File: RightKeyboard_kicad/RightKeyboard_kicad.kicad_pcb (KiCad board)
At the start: 2 copper layers, 139.8 x 88.1 mm, 37 parts, among them U1 Arduino_Pro_Micro

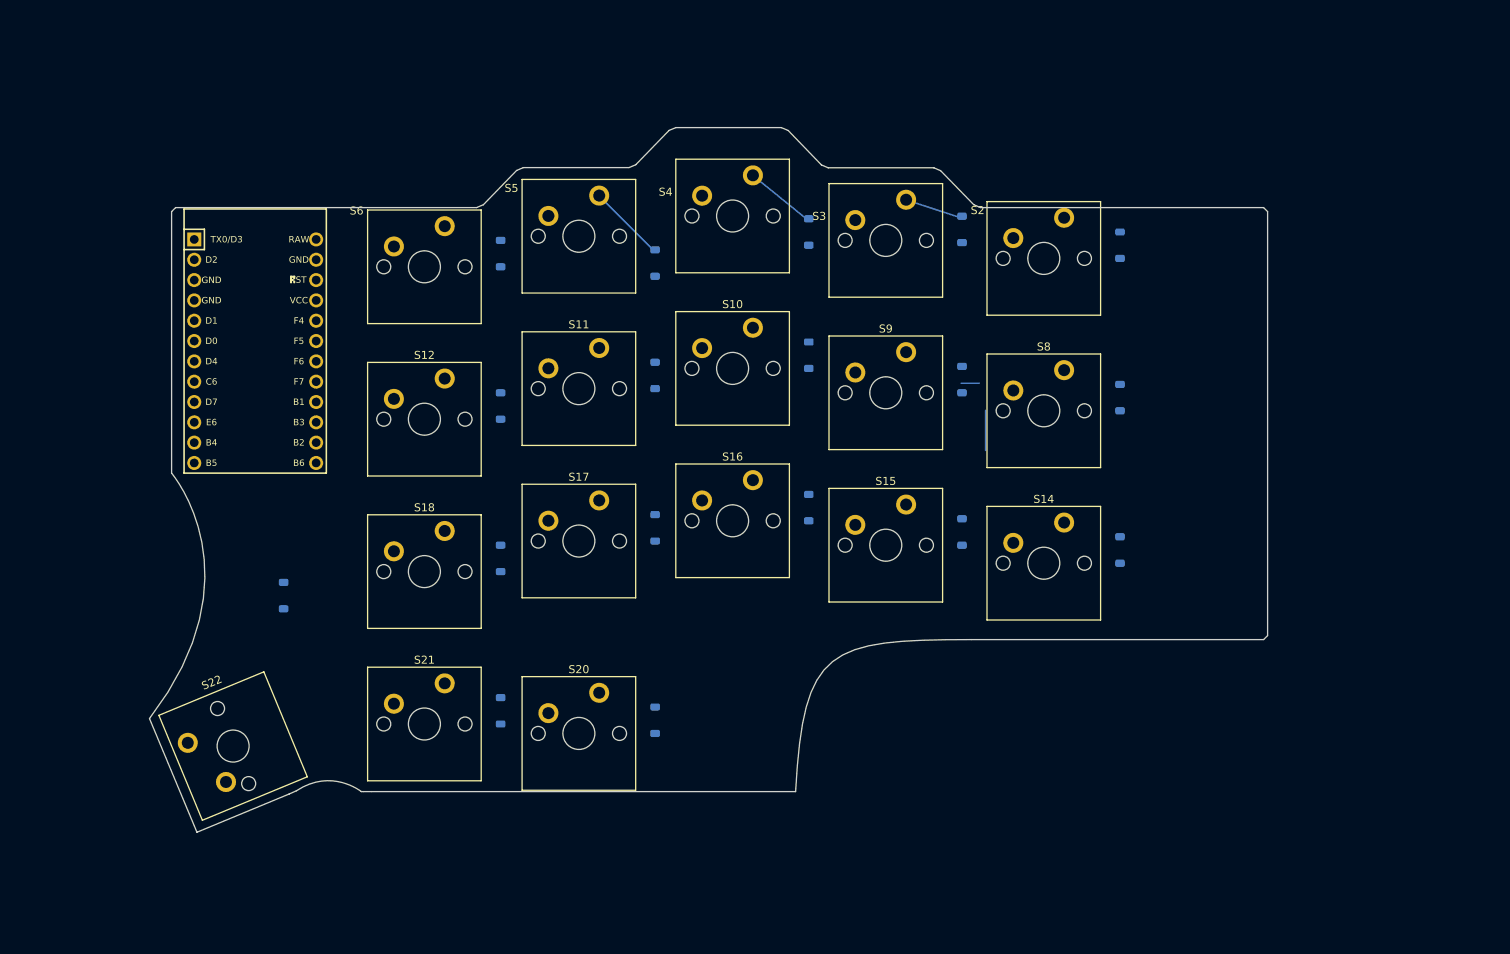
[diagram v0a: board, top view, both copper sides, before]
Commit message: Finished Right Keyboard PCB
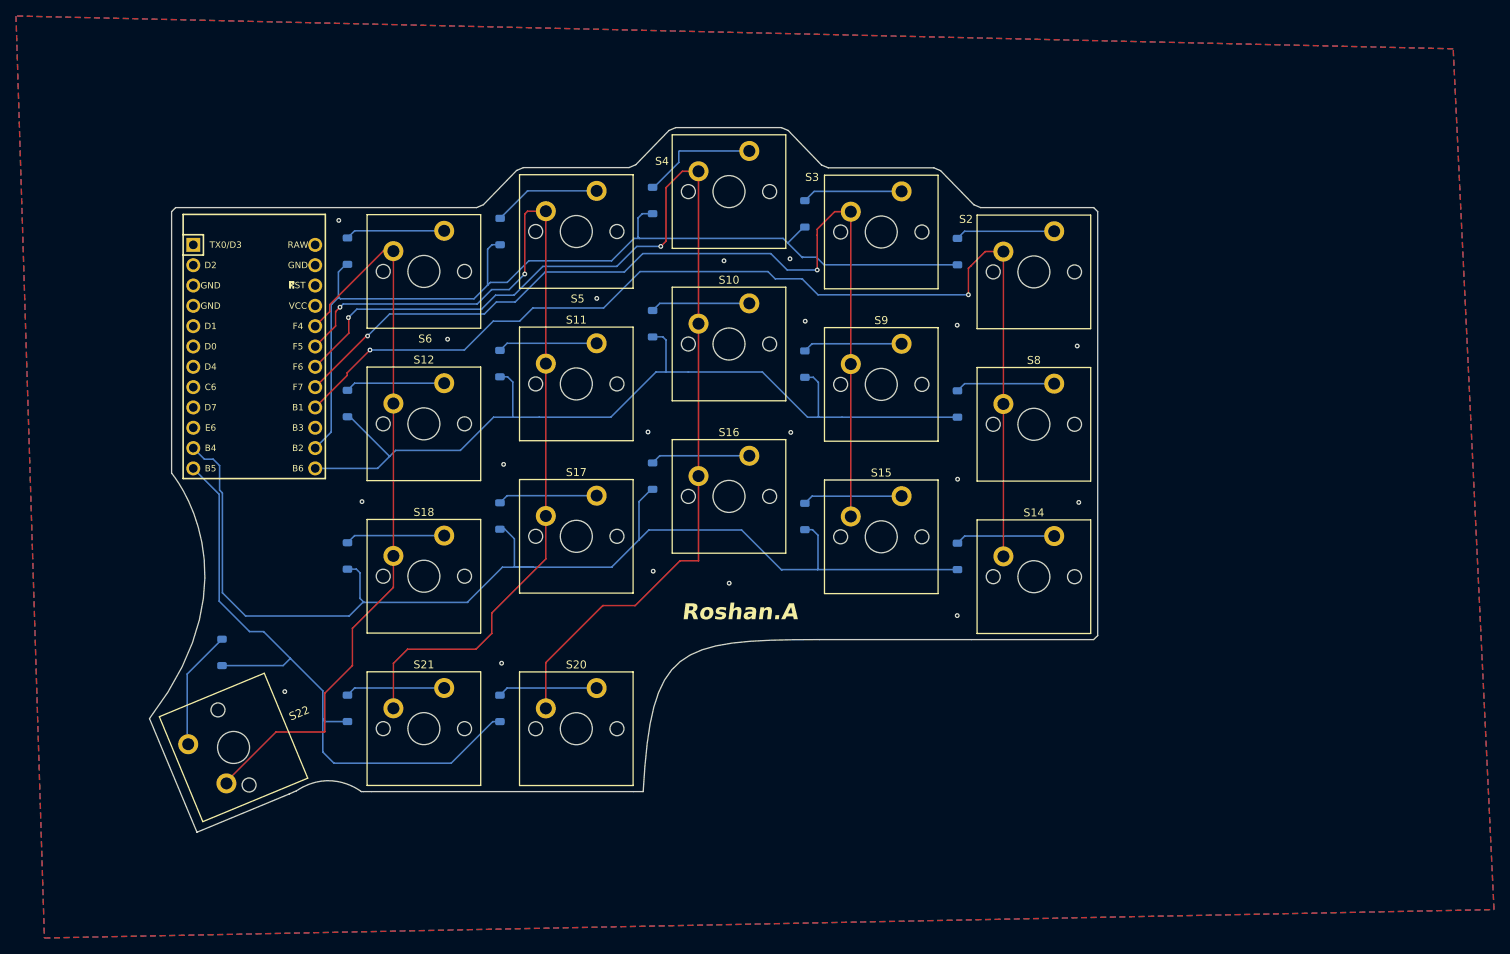
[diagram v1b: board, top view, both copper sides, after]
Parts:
- moved D14 20.3 mm to (165.4, 100.8)
- moved D2 20.3 mm to (165.4, 62.8)
- moved D8 20.3 mm to (165.4, 81.8)
- moved D10 19.9 mm to (127.3, 71.8)
- moved D16 19.9 mm to (127.3, 90.8)
- moved D4 19.9 mm to (127.3, 56.4)
- moved D5 19.8 mm to (108.3, 60.2)
- moved D15 19.7 mm to (146.4, 95.9)
- moved D3 19.7 mm to (146.4, 58.0)
- moved D9 19.7 mm to (146.4, 76.8)
- moved D11 19.5 mm to (108.2, 76.8)
- moved D17 19.5 mm to (108.2, 95.8)
- moved D20 19.5 mm to (108.2, 119.9)
- moved D12 19.1 mm to (89.2, 81.7)
- moved D18 19.1 mm to (89.2, 100.8)
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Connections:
- S10 pad 1: /Col4 -> /Col3
- S11 pad 1: /Col5 -> /Col2
- S12 pad 1: /Col6 -> /Col1
- S14 pad 1: /Col2 -> /Col5
- S15 pad 1: /Col3 -> /Col4
- S16 pad 1: /Col4 -> /Col3
- S17 pad 1: /Col5 -> /Col2
- S18 pad 1: /Col6 -> /Col1
- S2 pad 1: /Col2 -> /Col5
- S20 pad 1: /Col4 -> /Col3
- S21 pad 1: /Col5 -> /Col2
- S22 pad 1: /Col6 -> /Col1
- S3 pad 1: /Col3 -> /Col4
- S4 pad 1: /Col4 -> /Col3
- S5 pad 1: /Col5 -> /Col2
- S6 pad 1: /Col6 -> /Col1
- S8 pad 1: /Col2 -> /Col5
- S9 pad 1: /Col3 -> /Col4
- U1 pad 10: /Col6 -> unconnected-(U1-7/PE6-Pad10)
- U1 pad 11: /Row1 -> /Row3
- U1 pad 12: /Row2 -> /Row4
- U1 pad 13: unconnected-(U1-10/PB6-Pad13) -> /Row2
- U1 pad 14: unconnected-(U1-16/PB2-Pad14) -> /Row1
- U1 pad 15: /Row3 -> /Col6
- U1 pad 16: /Row4 -> /Col5
- U1 pad 17: unconnected-(U1-A0/PF7-Pad17) -> /Col4
- U1 pad 18: unconnected-(U1-A1/PF6-Pad18) -> /Col3
- U1 pad 19: unconnected-(U1-A2/PF5-Pad19) -> /Col2
- U1 pad 20: unconnected-(U1-A3/PF4-Pad20) -> /Col1
- U1 pad 23: unconnected-(U1-GND-Pad23) -> /GND
- U1 pad 3: /GND -> unconnected-(U1-GND-Pad3)
- U1 pad 5: /Col1 -> unconnected-(U1-2/PD1-Pad5)
- U1 pad 6: /Col2 -> unconnected-(U1-3/PD0-Pad6)
- U1 pad 7: /Col3 -> unconnected-(U1-4/PD4-Pad7)
- U1 pad 8: /Col4 -> unconnected-(U1-5/PC6-Pad8)
- U1 pad 9: /Col5 -> unconnected-(U1-6/PD7-Pad9)
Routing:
- net /Row3: track 0.00 -> 147.2 mm
- net /Col3: track 0.00 -> 141.9 mm, vias 0 -> 2
- net /Col5: track 0.00 -> 136.8 mm, vias 0 -> 2
- net /Row1: track 0.00 -> 120.7 mm
- net /Col4: track 0.00 -> 118.8 mm, vias 0 -> 2
- net /Col2: track 0.00 -> 116.3 mm, vias 0 -> 2
- net /Row2: track 0.00 -> 113.5 mm
- net /Col1: track 0.00 -> 92.9 mm
- net /Row4: track 0.00 -> 80.2 mm
- net Net-(D22-A): track 0.00 -> 15.0 mm
- net Net-(D4-A): track 0.00 -> 14.8 mm
- net Net-(D5-A): track 0.00 -> 13.5 mm
- net Net-(D3-A): track 0.00 -> 12.6 mm
- net Net-(D8-A): track 0.00 -> 12.5 mm
- net Net-(D11-A): track 0.00 -> 12.5 mm
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- added copper zone on B.Cu, net /GND
- added copper zone on F.Cu, net /GND
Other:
- board size 139.8 x 88.1 mm -> 118.5 x 88.1 mm
- board text added: "Roshan.A"
